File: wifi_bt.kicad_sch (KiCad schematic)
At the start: 37 parts, among them J3 U_FL-R-SMT-1, U26 WiFi_Bluetooth_LBEE5PK2AE, Y4 Oscillator_32.768kHz_ECS_2520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

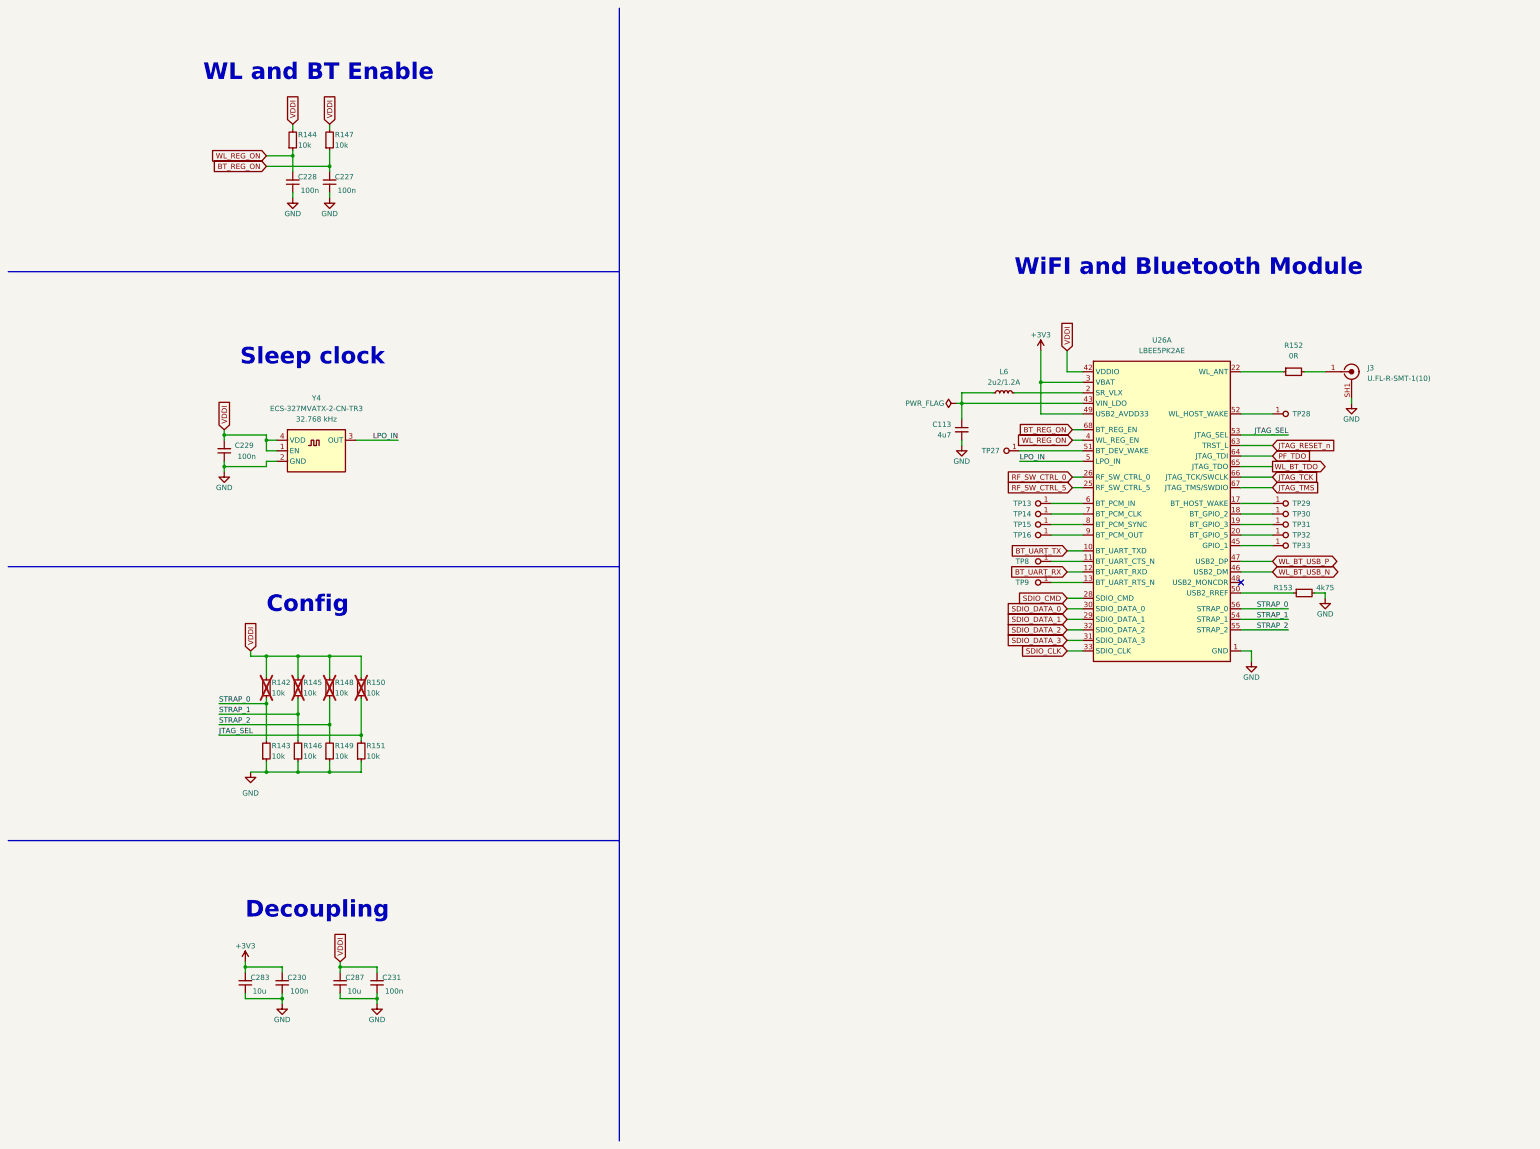
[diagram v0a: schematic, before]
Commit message: [#57505] Simplify config of WL_BT module, add level shifters
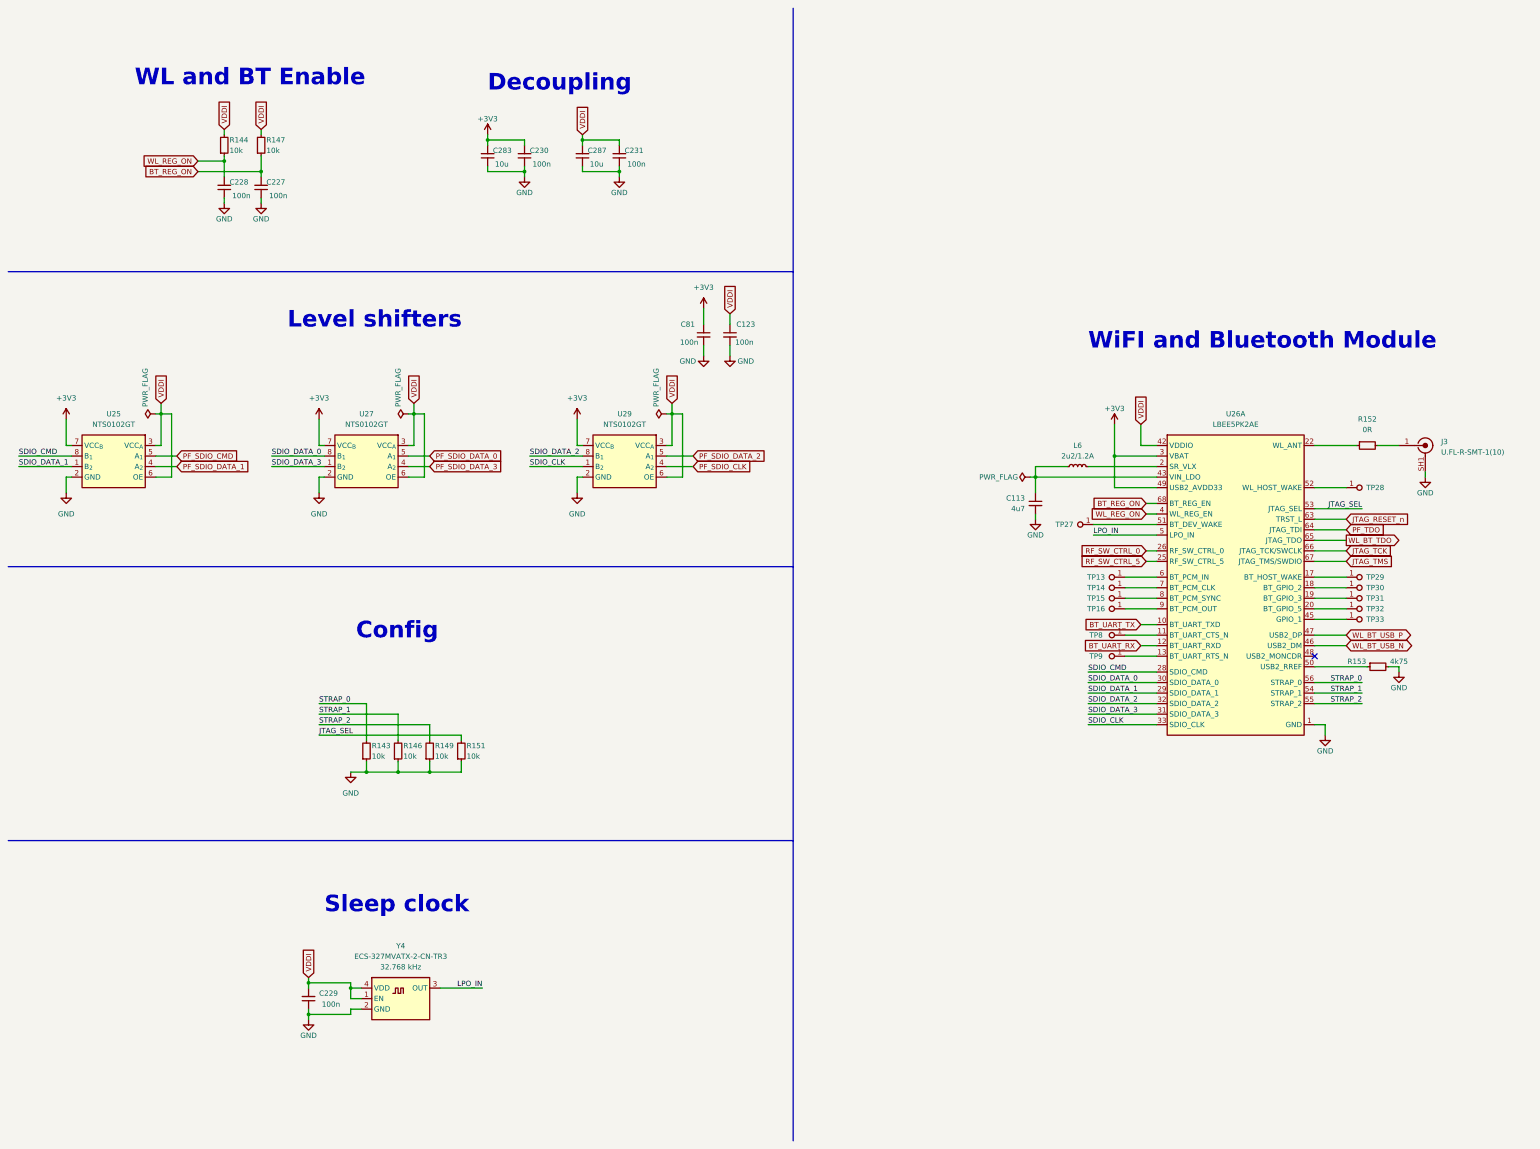
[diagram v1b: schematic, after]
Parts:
- removed R142, R145, R148, R150: R_10k_0402, antmicro-footprints:R_0402_1005Metric, symbol antmicroResistors0402:R_10k_0402
- added C123, C81: C_100n_0402, antmicro-footprints:C_0402_1005Metric, symbol antmicroCapacitors0402:C_100n_0402
- added U25, U27, U29: NTS0102_XSON, antmicro-footprints:XSON-8_1x1.95mm_P0.5mm, symbol antmicroLogicTranslatorsLevelShifters:NTS0102_XSON
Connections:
- net +3V3: now also C81.1, U25.7 (VCC_{B}), U27.7 (VCC_{B}), U29.7 (VCC_{B})
- net GND: now also C123.2, C81.2, U25.2 (GND), U27.2 (GND), U29.2 (GND)
- net SDIO_CLK: now also U29.1 (B_{2})
- net SDIO_CMD: now also U25.8 (B_{1})
- net SDIO_DATA_0: now also U27.8 (B_{1})
- net SDIO_DATA_1: now also U25.1 (B_{2})
- net SDIO_DATA_2: now also U29.8 (B_{1})
- net SDIO_DATA_3: now also U27.1 (B_{2})
- net VDDI: now also C123.1, U25.3 (VCC_{A}), U25.6 (OE), U27.3 (VCC_{A}), U27.6 (OE), U29.3 (VCC_{A}), U29.6 (OE)
- new net PF_SDIO_CLK: U29.4 (A_{2})
- new net PF_SDIO_CMD: U25.5 (A_{1})
- new net PF_SDIO_DATA_0: U27.5 (A_{1})
- new net PF_SDIO_DATA_1: U25.4 (A_{2})
- new net PF_SDIO_DATA_2: U29.5 (A_{1})
- new net PF_SDIO_DATA_3: U27.4 (A_{2})
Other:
- note added: "Level shifters"
- moved on the sheet: C113, C227, C228, C229, C230, C231, C283, C287, J3, L6, R143, R144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

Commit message: [#57505] Continue migration to hierarchical schematic
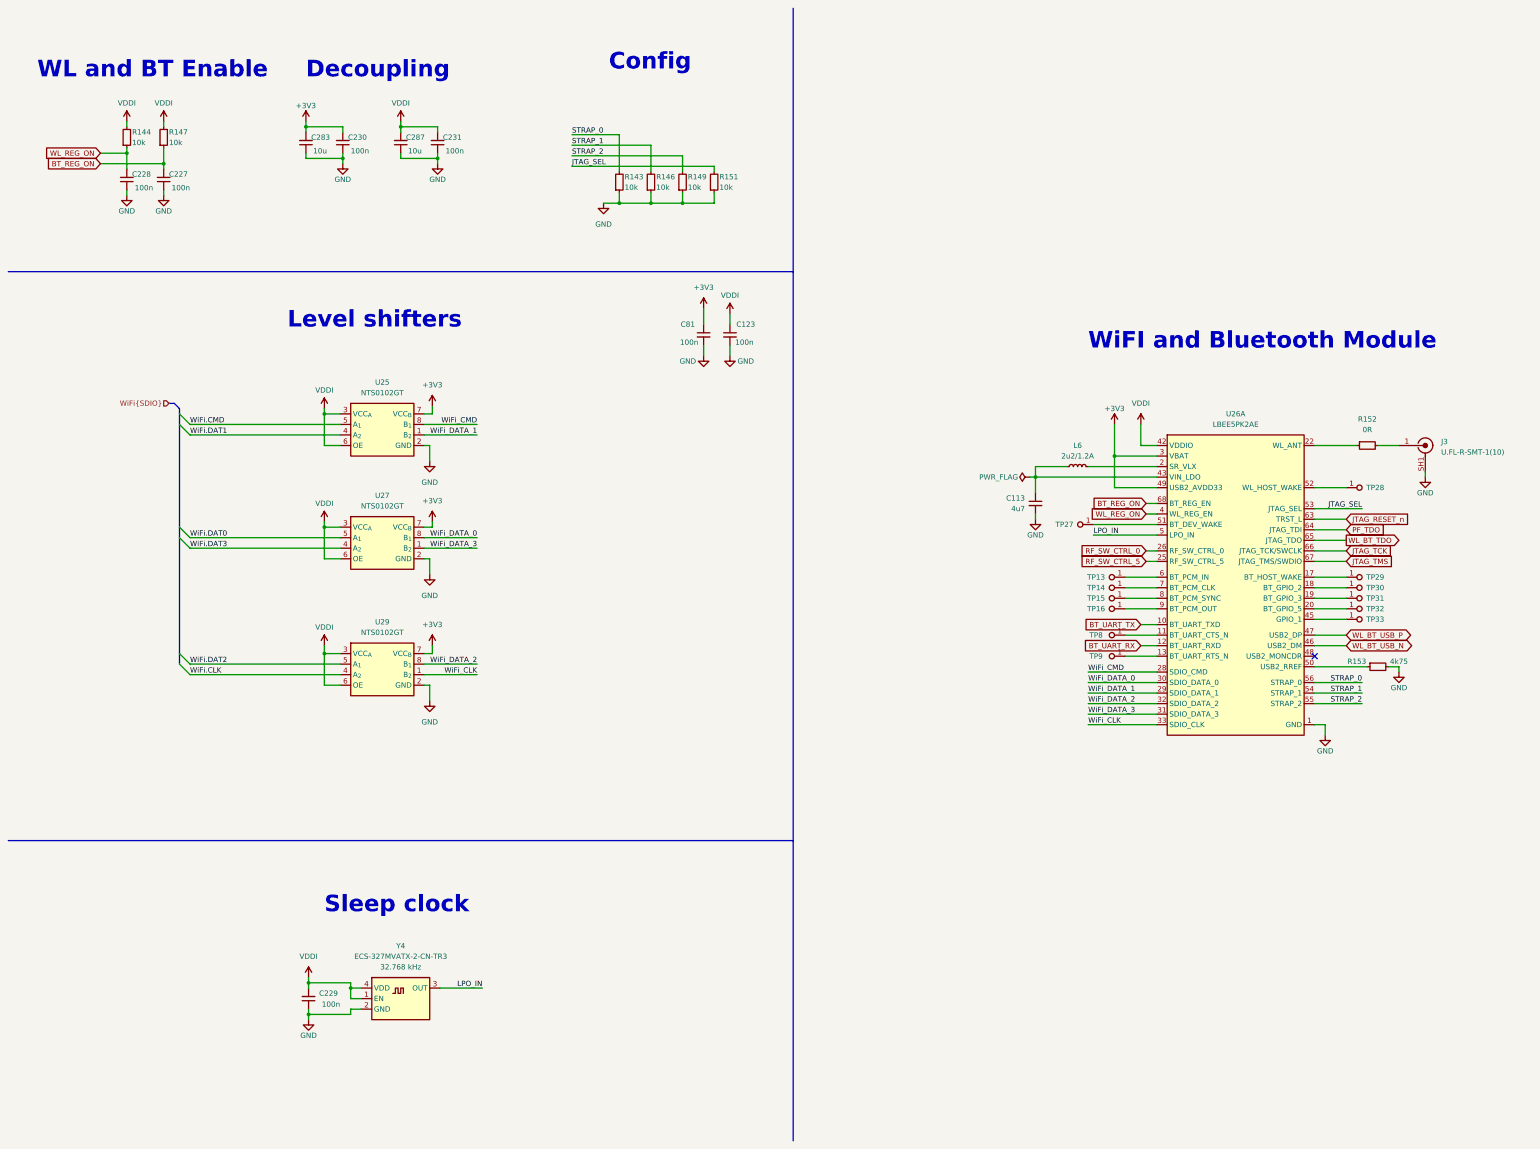
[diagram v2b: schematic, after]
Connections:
- net PF_SDIO_CLK renamed WiFi.CLK
- net PF_SDIO_CMD renamed WiFi.CMD
- net PF_SDIO_DATA_0 renamed WiFi.DAT0
- net PF_SDIO_DATA_1 renamed WiFi.DAT1
- net PF_SDIO_DATA_2 renamed WiFi.DAT2
- net PF_SDIO_DATA_3 renamed WiFi.DAT3
- net SDIO_CLK renamed WiFi_CLK
- net SDIO_CMD renamed WiFi_CMD
- net SDIO_DATA_0 renamed WiFi_DATA_0
- net SDIO_DATA_1 renamed WiFi_DATA_1
- net SDIO_DATA_2 renamed WiFi_DATA_2
- net SDIO_DATA_3 renamed WiFi_DATA_3
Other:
- moved on the sheet: C227, C228, C230, C231, C283, C287, R143, R144, R146, R147, R149, R151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

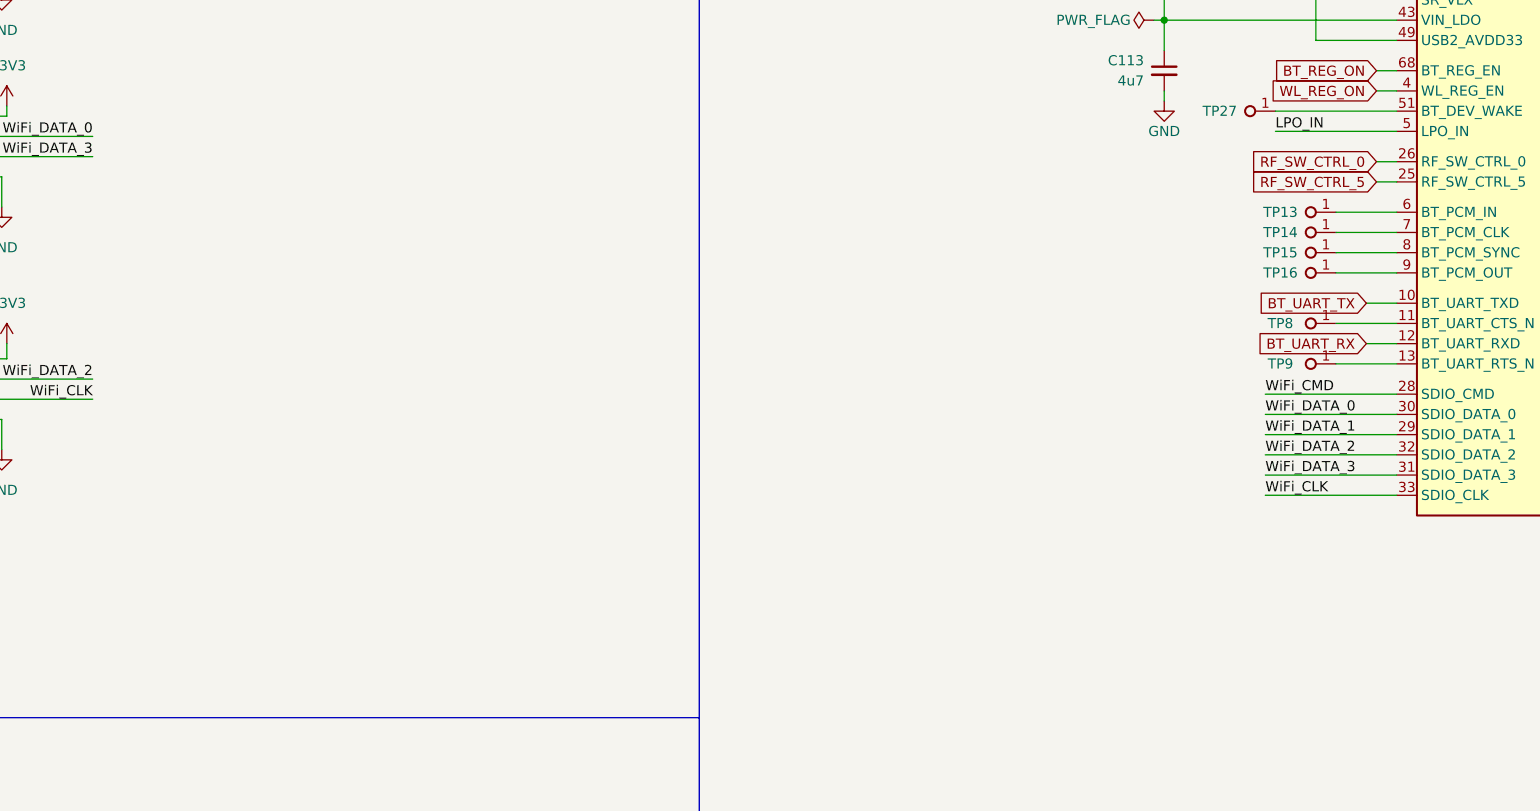
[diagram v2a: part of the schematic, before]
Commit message: [#57422] Add ETH PHY strap, WL_BT UART level shifter, fiducials, remove BYP_EN
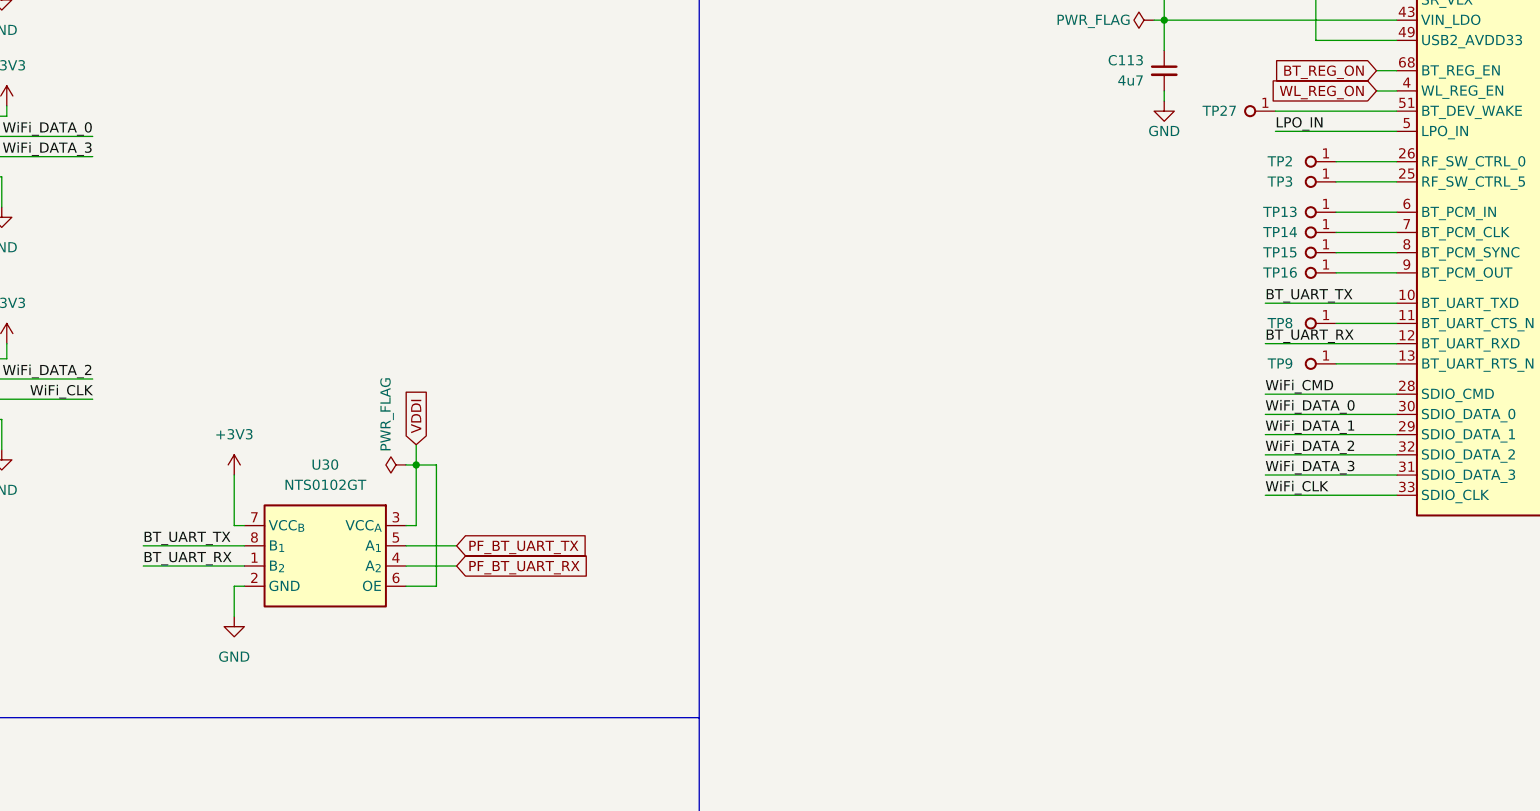
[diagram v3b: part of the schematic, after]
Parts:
- added TP2, TP3: TP_0.75mm_SMD, antmicro-footprints:TP_SMD_0.75mm, symbol antmicroTestPoints:TP_0.75mm_SMD
- added U30: NTS0102_XSON, antmicro-footprints:XSON-8_1x1.95mm_P0.5mm, symbol antmicroLogicTranslatorsLevelShifters:NTS0102_XSON
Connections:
- net +3V3: now also U30.7 (VCC_{B})
- net BT_UART_RX: now also U30.1 (B_{2})
- net BT_UART_TX: now also U30.8 (B_{1})
- net GND: now also U30.2 (GND)
- net VDDI: now also U30.3 (VCC_{A}), U30.6 (OE)
- net RF_SW_CTRL_0: no longer names the net of U26.26 (RF_SW_CTRL_0)
- net RF_SW_CTRL_0: now also TP2.1
- net RF_SW_CTRL_5: no longer names the net of U26.25 (RF_SW_CTRL_5)
- net RF_SW_CTRL_5: now also TP3.1
- new net PF_BT_UART_RX: U30.4 (A_{2})
- new net PF_BT_UART_TX: U30.5 (A_{1})

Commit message: [#57505] Finish defining buses
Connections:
- net +3V3: now also C231.2, C287.2, R144.2, R147.2
- net VDDI: no longer C231.2, C287.2, R144.2, R147.2
- net PF_BT_UART_RX renamed PF_BT.RX
- net PF_BT_UART_TX renamed PF_BT.TX
- net WL_BT_USB_N renamed WL_BT.D_N
- net WL_BT_USB_P renamed WL_BT.D_P
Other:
- moved on the sheet: U25, U27, U29, U30
